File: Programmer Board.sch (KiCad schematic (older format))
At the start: 3 parts, among them J1 105-1103-001, J2 Conn_01x03, J3 105-1102-001

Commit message: completed connections
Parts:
- added J?: Conn_01x02, symbol Connector_Generic:Conn_01x02
- added J?: Conn_02x18_Odd_Even, symbol Connector_Generic:Conn_02x18_Odd_Even
- added JP?: JUMPER-SMT_3_1-NC, SMT-JUMPER_3_1-NC, symbol SparkFun-Jumpers:JUMPER-SMT_3_1-NC
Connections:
- net Card Edge Conn/HEADER1.1: now also J?.9 (Pin_9)
- net Card Edge Conn/HEADER1.10: now also J?.25 (Pin_25)
- net Card Edge Conn/HEADER1.2: now also J?.11 (Pin_11)
- net Card Edge Conn/HEADER1.3: now also J?.13 (Pin_13)
- net Card Edge Conn/HEADER1.4: now also J?.15 (Pin_15)
- net Card Edge Conn/HEADER1.5: now also J?.17 (Pin_17)
- net Card Edge Conn/HEADER1.6: now also J?.19 (Pin_19)
- net Card Edge Conn/HEADER1.7: now also J?.21 (Pin_21)
- net Card Edge Conn/HEADER1.9: now also J?.23 (Pin_23)
- net Card Edge Conn/J5.2: now also J?.29 (Pin_29)
- net Card Edge Conn/J5.3: now also J?.31 (Pin_31)
- net Card Edge Conn/SW1.1: now also J?.1 (Pin_1)
- net Card Edge Conn/SW1.2: now also J?.3 (Pin_3)
- net Card Edge Conn/SW1.3: now also J?.5 (Pin_5)
- net Card Edge Conn/SW1.4: now also J?.7 (Pin_7)
- net Card Edge Conn/U21.20-DCLK: now also J?.33 (Pin_33)
- net Card Edge Conn/U22.3: now also J?.35 (Pin_35)
- net Card Edge Conn/U3.18: now also J?.27 (Pin_27)
- net Card Edge Conn/U3.19: now also JP?.3
- net GND: now also J?.10 (Pin_10), J?.12 (Pin_12), J?.14 (Pin_14), J?.16 (Pin_16), J?.18 (Pin_18), J?.2 (Pin_2), J?.20 (Pin_20), J?.22 (Pin_22), J?.24 (Pin_24), J?.26 (Pin_26), J?.28 (Pin_28), J?.30 (Pin_30), J?.32 (Pin_32), J?.34 (Pin_34), J?.36 (Pin_36), J?.4 (Pin_4), J?.6 (Pin_6), J?.8 (Pin_8)
- net USB to UART/UART2.RXD: now also J?.2 (Pin_2)
- net USB to UART/UART2.TXD: now also JP?.2
- new net: J?.1 (Pin_1), JP?.1
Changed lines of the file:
@@
 F0 "Card Edge Conn" 50
 F1 "CardEdgeConn.sch" 50
-F2 "U21.20-DCLK" I L 7350 1550 50
-F3 "SW1.1" I L 7350 1700 50
-F4 "GPS.TXD" I L 7350 1800 50
-F5 "U22.3" I L 7350 1900 50
-F6 "J5.3" I L 7350 2000 50
-F7 "SW1.3" I L 7350 2100 50
-F8 "U3.18" I L 7350 2200 50
-F9 "GPS.RXD" I L 7350 2300 50
-F10 "U3.19" I L 7350 2400 50
-F11 "SW1.2" I R 10050 1600 50
+F2 "U21.20-DCLK" I R 10050 3000 50
+F3 "SW1.1" I R 10050 1400 50
+F4 "GPS.TXD" I L 7350 2500 50
+F5 "U22.3" I R 10050 3100 50
+F6 "J5.3" I R 10050 2900 50
+F7 "SW1.3" I R 10050 1600 50
+F8 "U3.18" I R 10050 2700 50
+F9 "GPS.RXD" I L 7350 2600 50
+F10 "U3.19" I L 7350 2950 50
+F11 "SW1.2" I R 10050 1500 50
 F12 "SW1.4" I R 10050 1700 50
-F13 "J5.2" I R 10050 1800 50
-F14 "HEADER1.1" I R 10050 2200 50
-F15 "HEADER1.2" I R 10050 2300 50
-F16 "HEADER1.3" I R 10050 2400 50
-F17 "HEADER1.4" I R 10050 2500 50
-F18 "HEADER1.5" I R 10050 2600 50
-F19 "HEADER1.6" I R 10050 2700 50
-F20 "HEADER1.7" I R 10050 2800 50
-F21 "HEADER1.9" I R 10050 2900 50
-F22 "HEADER1.10" I R 10050 3000 50
+F13 "J5.2" I R 10050 2800 50
+F14 "HEADER1.1" I R 10050 1800 50
+F15 "HEADER1.2" I R 10050 1900 50
+F16 "HEADER1.3" I R 10050 2000 50
+F17 "HEADER1.4" I R 10050 2100 50
+F18 "HEADER1.5" I R 10050 2200 50
+F19 "HEADER1.6" I R 10050 2300 50
+F20 "HEADER1.7" I R 10050 2400 50
+F21 "HEADER1.9" I R 10050 2500 50
+F22 "HEADER1.10" I R 10050 2600 50
 F23 "9V_PS" I L 7350 1350 50
 $EndSheet
+Wire Wire Line
+	4300 2500 7350 2500
+Wire Wire Line
+	4300 2600 7350 2600
+$Comp
+L SparkFun-Jumpers:JUMPER-SMT_3_1-NC JP?
+U 1 1 5F8F06E0
+P 5100 2950
+AR Path="/5F7C6408/5F8F06E0" Ref="JP?"  Part="1"
+AR Path="/5F8F06E0" Ref="JP?"  Part="1"
+F 0 "JP?" H 5204 3045 45  0000 L CNN
+F 1 "JUMPER-SMT_3_1-NC" H 5204 2961 45  0000 L CNN
+F 2 "SMT-JUMPER_3_1-NC" H 5100 3200 20  0001 C CNN
+F 3 "" V 5100 2895 60  0001 C CNN
+F 4 "XXX-00000" H 5204 2866 60  0000 L CNN "PROD_ID"
+	1    5100 2950
+	0    -1   1    0
+$EndComp
+Wire Wire Line
+	4300 2800 5100 2800
+Wire Wire Line
+	5300 2950 7350 2950
+$Comp
+L Connector_Generic:Conn_01x02 J?
+U 1 1 5F8F12C1
+P 4500 3450
+F 0 "J?" V 4372 3530 50  0000 L CNN
+F 1 "Conn_01x02" V 4463 3530 50  0000 L CNN
+F 2 "" H 4500 3450 50  0001 C CNN
+F 3 "~" H 4500 3450 50  0001 C CNN
+	1    4500 3450
+	0    1    1    0
+$EndComp
+Wire Wire Line
+	4500 3250 4500 2950
+Wire Wire Line
+	4500 2950 4900 2950
+Wire Wire Line
+	4400 3250 4400 2700
+Wire Wire Line
+	4400 2700 4300 2700
+$Comp
+L Connector_Generic:Conn_02x18_Odd_Even J?
+U 1 1 5F8F3B51
+P 10450 2200
+F 0 "J?" H 10500 3217 50  0000 C CNN
+F 1 "Conn_02x18_Odd_Even" H 10500 3126 50  0000 C CNN
+F 2 "" H 10450 2200 50  0001 C CNN
+F 3 "~" H 10450 2200 50  0001 C CNN
+	1    10450 2200
+	1    0    0    -1
+$EndComp
+Wire Wire Line
+	10250 1400 10050 1400
+Wire Wire Line
+	10050 1500 10250 1500
+Wire Wire Line
+	10250 1600 10050 1600
+Wire Wire Line
+	10050 1700 10250 1700
+Wire Wire Line
+	10250 1800 10050 1800
+Wire Wire Line
+	10050 1900 10250 1900
+Wire Wire Line
+	10250 2000 10050 2000
+Wire Wire Line
+	10050 2100 10250 2100
+Wire Wire Line
+	10250 2200 10050 2200
+Wire Wire Line
+	10050 2300 10250 2300
+Wire Wire Line
+	10250 2400 10050 2400
+Wire Wire Line
+	10050 2500 10250 2500
+Wire Wire Line
+	10250 2600 10050 2600
+Wire Wire Line
+	10050 2700 10250 2700
+Wire Wire Line
+	10250 2800 10050 2800
+Wire Wire Line
+	10050 2900 10250 2900
+Wire Wire Line
+	10250 3000 10050 3000
+Wire Wire Line
+	10050 3100 10250 3100
+$Comp
+L power:GND #PWR?
+U 1 1 5F8FB83E
+P 10850 3150
+F 0 "#PWR?" H 10850 2900 50  0001 C CNN
+F 1 "GND" H 10855 2977 50  0000 C CNN
+F 2 "" H 10850 3150 50  0001 C CNN
+F 3 "" H 10850 3150 50  0001 C CNN
+	1    10850 3150
+	1    0    0    -1
+$EndComp
+Wire Wire Line
+	10850 3150 10850 3100
+Wire Wire Line
+	10850 3100 10750 3100
+Wire Wire Line
+	10750 1400 10850 1400
+Connection ~ 10850 3100
+Wire Wire Line
+	10750 3000 10850 3000
+Connection ~ 10850 3000
+Wire Wire Line
+	10850 3000 10850 3100
+Wire Wire Line
+	10750 2900 10850 2900
+Connection ~ 10850 2900
+Wire Wire Line
+	10850 2900 10850 3000
+Wire Wire Line
+	10750 2800 10850 2800
+Connection ~ 10850 2800
+Wire Wire Line
+	10850 2800 10850 2900
+Wire Wire Line
+	10750 2700 10850 2700
+Connection ~ 10850 2700
+Wire Wire Line
+	10850 2700 10850 2800
+Wire Wire Line
+	10750 2600 10850 2600
+Connection ~ 10850 2600
+Wire Wire Line
+	10850 2600 10850 2700
+Wire Wire Line
+	10750 2500 10850 2500
+Connection ~ 10850 2500
+Wire Wire Line
+	10850 2500 10850 2600
+Wire Wire Line
+	10750 2400 10850 2400
+Connection ~ 10850 2400
+Wire Wire Line
+	10850 2400 10850 2500
+Wire Wire Line
+	10750 2300 10850 2300
+Wire Wire Line
+	10850 1400 10850 1500
+Connection ~ 10850 2300
+Wire Wire Line
+	10850 2300 10850 2400
+Wire Wire Line
+	10750 2200 10850 2200
+Connection ~ 10850 2200
+Wire Wire Line
+	10850 2200 10850 2300
+Wire Wire Line
+	10750 2100 10850 2100
+Connection ~ 10850 2100
+Wire Wire Line
+	10850 2100 10850 2200
+Wire Wire Line
+	10750 2000 10850 2000
+Connection ~ 10850 2000
+Wire Wire Line
+	10850 2000 10850 2100
+Wire Wire Line
+	10750 1900 10850 1900
+Connection ~ 10850 1900
+Wire Wire Line
+	10850 1900 10850 2000
+Wire Wire Line
+	10750 1800 10850 1800
+Connection ~ 10850 1800
+Wire Wire Line
+	10850 1800 10850 1900
+Wire Wire Line
+	10750 1700 10850 1700
+Connection ~ 10850 1700
+Wire Wire Line
+	10850 1700 10850 1800
+Wire Wire Line
+	10750 1600 10850 1600
+Connection ~ 10850 1600
+Wire Wire Line
+	10850 1600 10850 1700
+Wire Wire Line
+	10750 1500 10850 1500
+Connection ~ 10850 1500
+Wire Wire Line
+	10850 1500 10850 1600
 $EndSCHEMATC

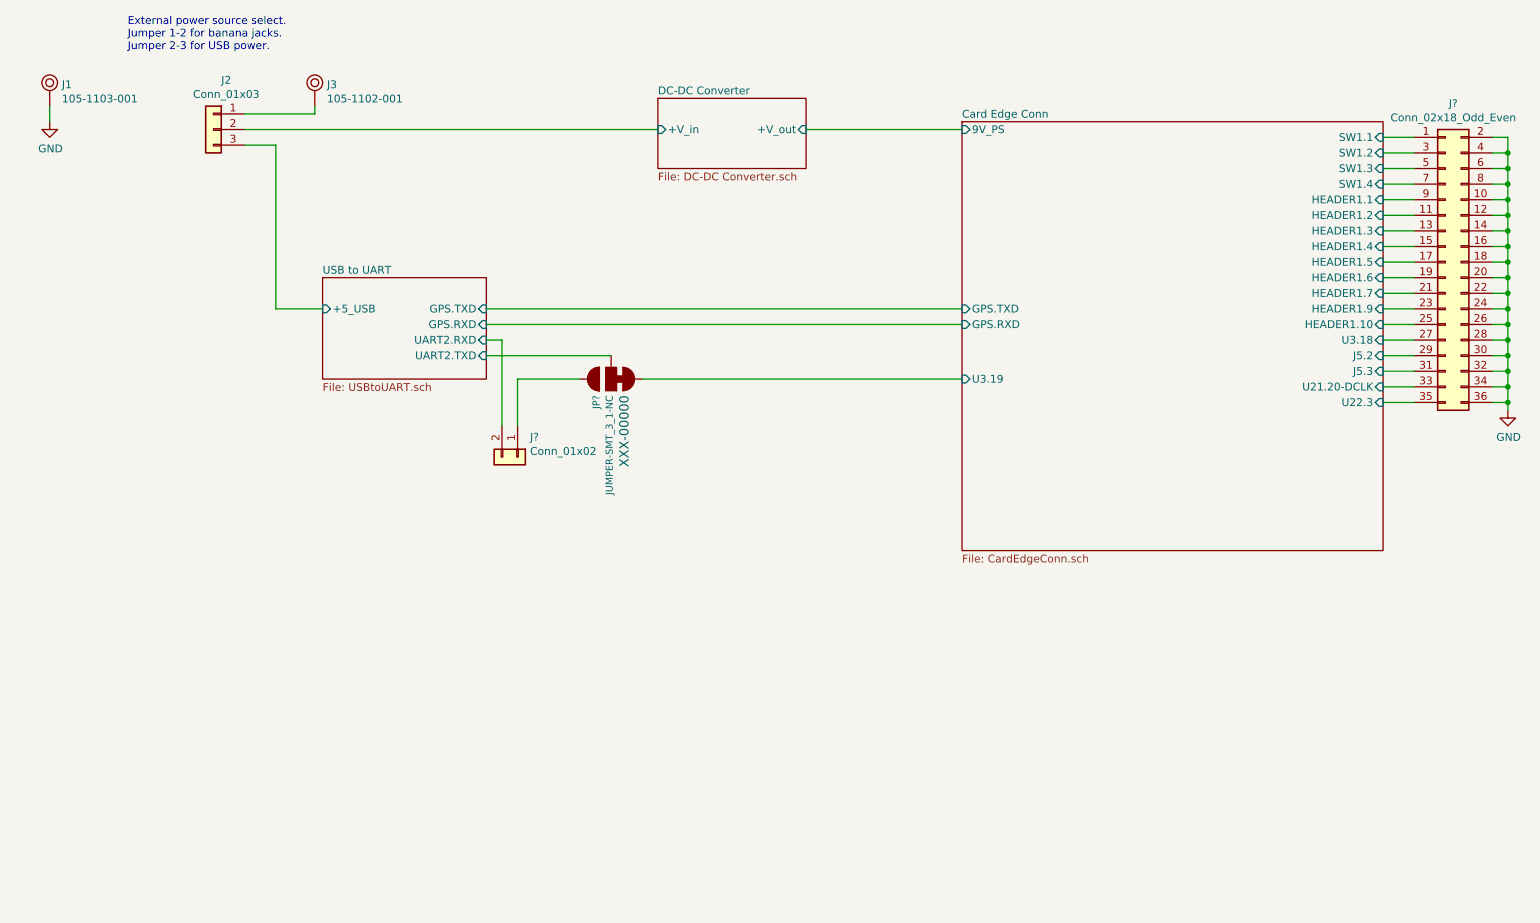
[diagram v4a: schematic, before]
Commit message: eFuse added
Added eFuse, LEDs, and addtional power configuration options.
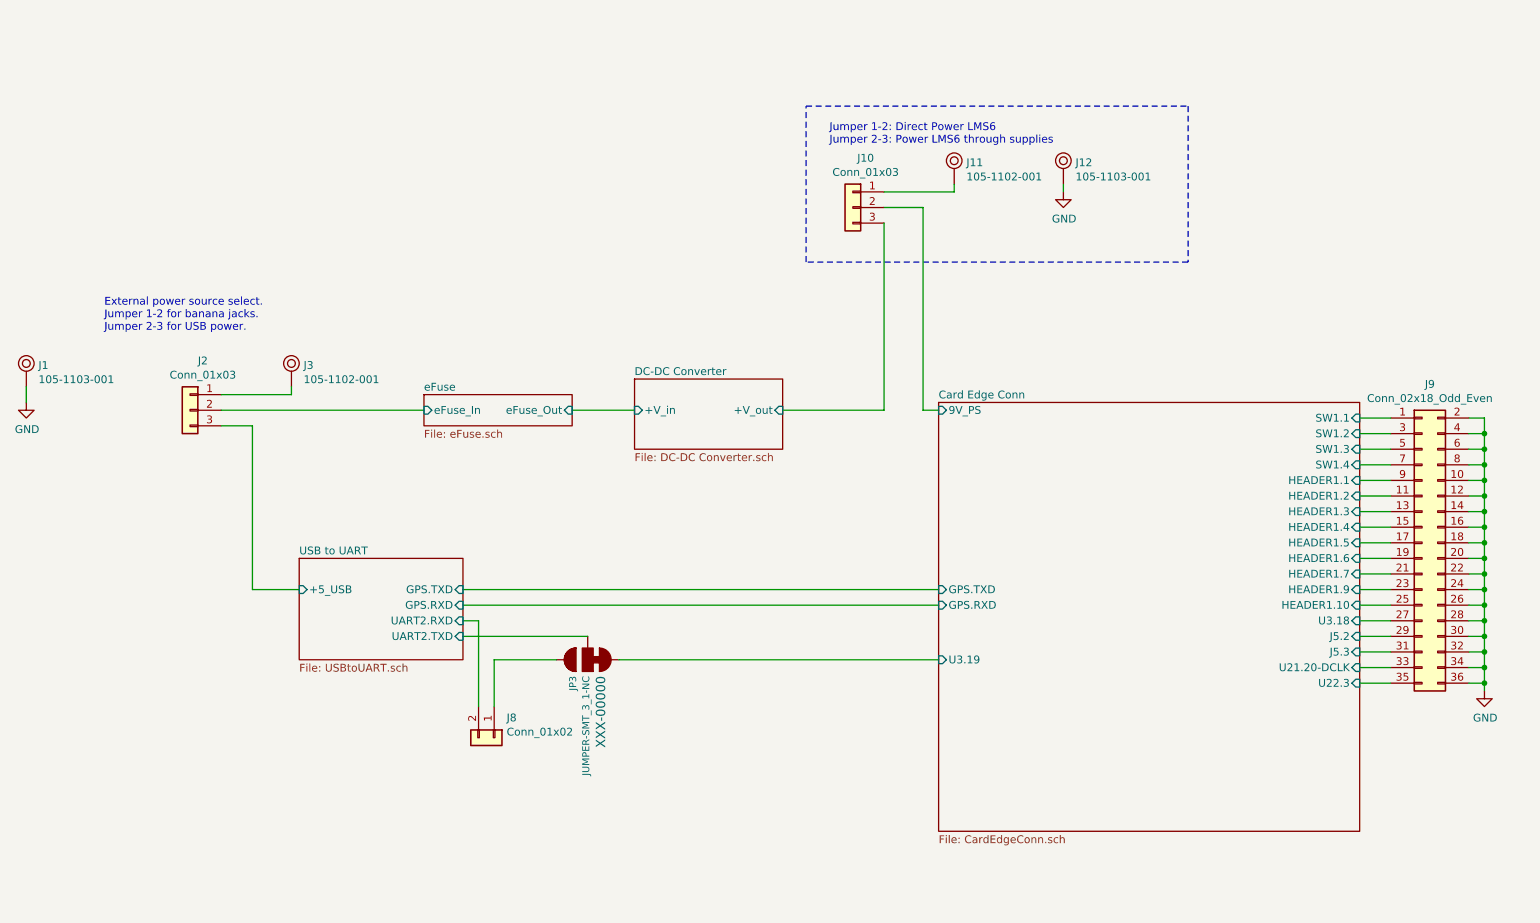
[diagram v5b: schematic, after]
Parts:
- added J10: Conn_01x03, Connector_PinHeader_2.54mm:PinHeader_1x03_P2.54mm_Vertical, symbol Connector_Generic:Conn_01x03
- added J11: 105-1102-001, digikey-footprints:Test_Jack_Horiz, symbol dk_Banana-and-Tip-Connectors-Jacks-Plugs:105-1102-001
- added J12: 105-1103-001, digikey-footprints:Test_Jack_Horiz, symbol dk_Banana-and-Tip-Connectors-Jacks-Plugs:105-1103-001
- J2: footprint (none) -> Connector_PinHeader_2.54mm:PinHeader_1x03_P2.54mm_Vertical; MPN (none) -> 61300311121; Manufacturer (none) -> Würth Elektronik
- J8: renamed from J?; footprint (none) -> Connector_PinHeader_2.54mm:PinHeader_1x02_P2.54mm_Vertical; MPN (none) -> 61300211121; Manufacturer (none) -> Würth Elektronik
- J9: renamed from J?; footprint (none) -> Connector_PinHeader_2.54mm:PinHeader_2x18_P2.54mm_Vertical; MPN (none) -> PREC020DAAN-RC; Manufacturer (none) -> Sullins Connector Solutions
- gave numbers to parts that had none: 1
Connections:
- net Card Edge Conn/9V_PS: now also J10.2 (Pin_2)
- net DC-DC Converter/+V_in: no longer J2.2 (Pin_2)
- net GND: now also J12.1
- new net: J10.1 (Pin_1), J11.1
- new net DC-DC Converter/+V_out: J10.3 (Pin_3)
- new net eFuse/eFuse_In: J2.2 (Pin_2)
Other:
- note added: "Jumper 1-2: Direct Power LMS6\nJumper 2-3: Power LMS6 through supplies"
- moved on the sheet: J1, J2, J3, J8, J9, JP3
